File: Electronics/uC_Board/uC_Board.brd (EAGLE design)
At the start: 30.8 x 54.6 mm, 11 parts, among them IC1 74LS241N, J1 1, J2 SCREW-TERMINAL-2P-3470070P1, J3 2, J4 3

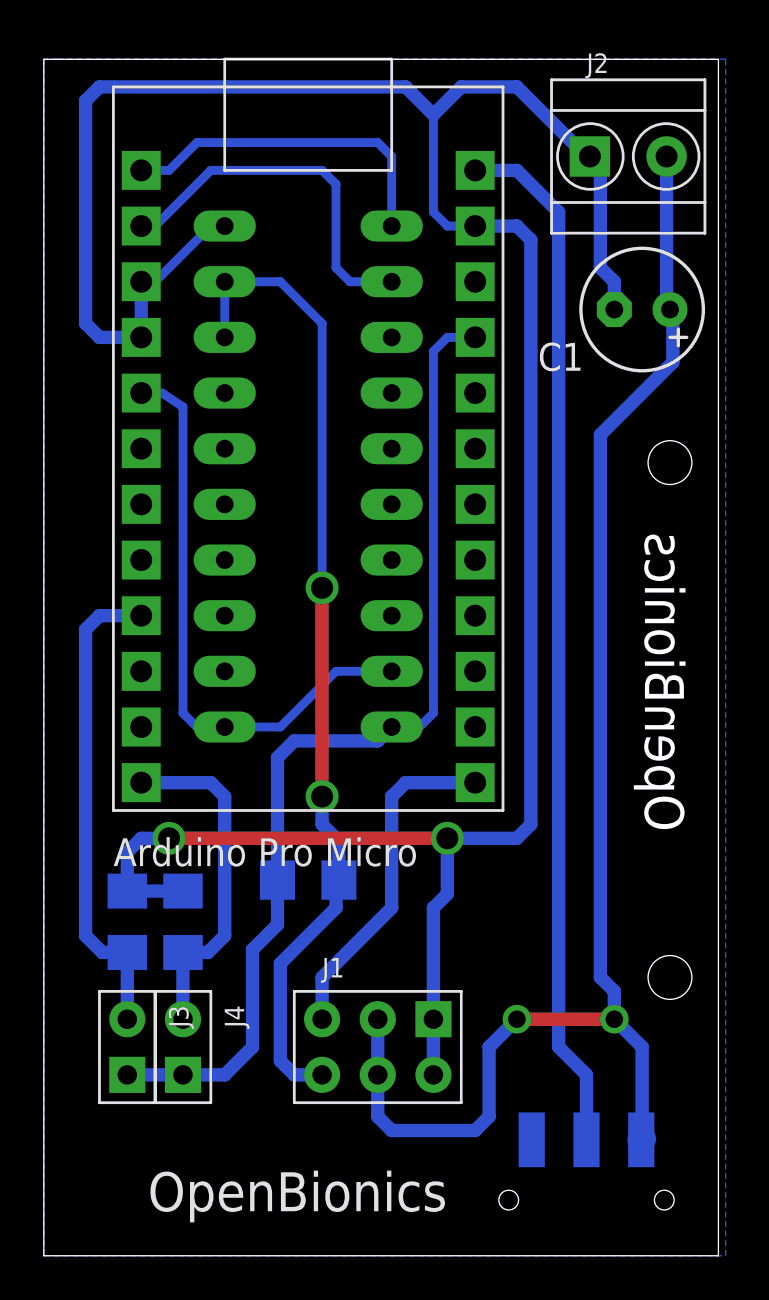
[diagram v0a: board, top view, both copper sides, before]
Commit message: Repair the Bottom Silkscreen of uC_Board PCB.
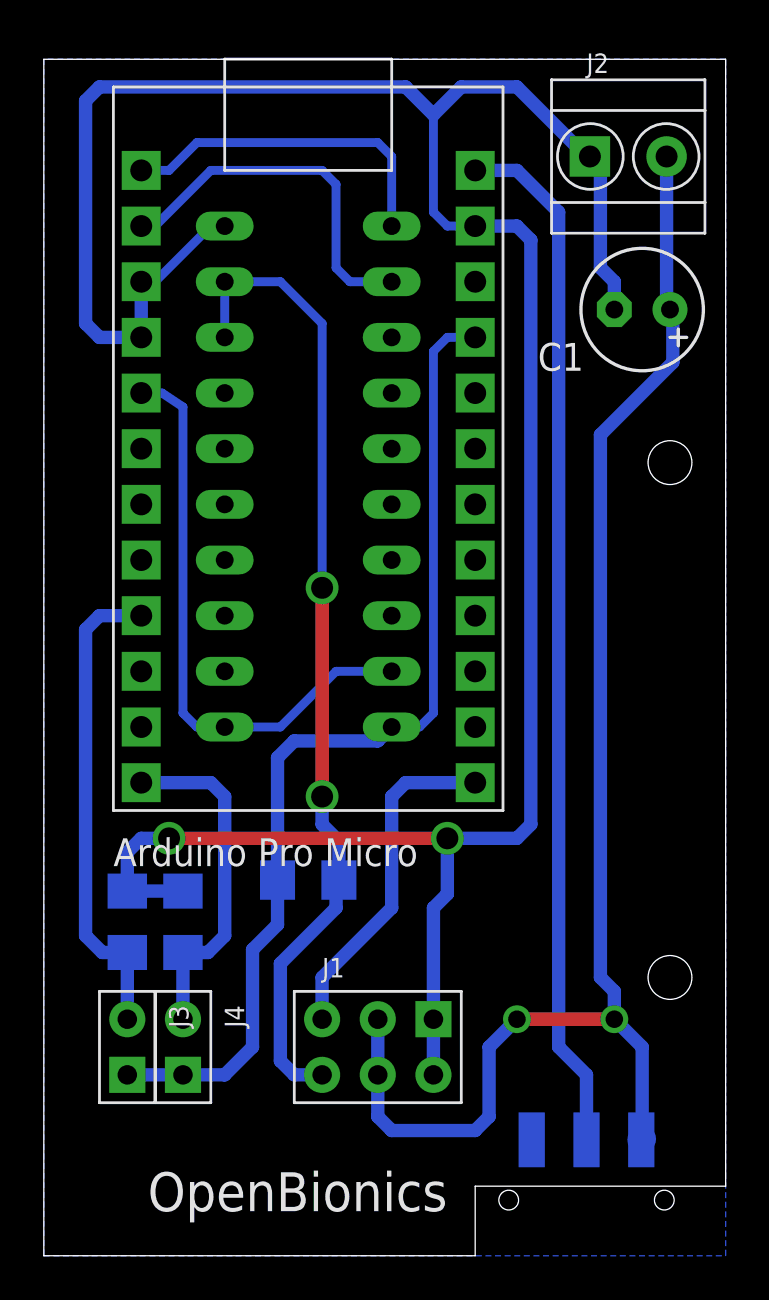
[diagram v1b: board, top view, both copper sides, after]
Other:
- board size 30.8 x 54.6 mm -> 31.1 x 54.6 mm
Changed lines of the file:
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@@
 <?xml version="1.0" encoding="utf-8"?>
 <!DOCTYPE eagle SYSTEM "eagle.dtd">
-<eagle version="7.1.0">
+<eagle version="7.2.0">
 <drawing>
 <settings>
@@
 <board>
 <plain>
-<wire x1="35.56" y1="15.24" x2="66.345" y2="15.24" width="0" layer="20"/>
-<wire x1="66.345" y1="15.24" x2="66.345" y2="69.84" width="0" layer="20"/>
-<wire x1="66.345" y1="69.84" x2="35.56" y2="69.84" width="0" layer="20"/>
+<wire x1="66.6625" y1="69.84" x2="35.56" y2="69.84" width="0" layer="20"/>
 <wire x1="35.56" y1="69.84" x2="35.56" y2="15.24" width="0" layer="20"/>
 <hole x="64.135" y="51.435" drill="2"/>
 <hole x="64.135" y="27.94" drill="2"/>
-<text x="64.77" y="48.26" size="1.778" layer="20" font="vector" ratio="18" rot="MR270">OpenBionics</text>
+<text x="64.77" y="48.26" size="1.778" layer="22" font="vector" ratio="18" rot="MR270">OpenBionics</text>
 <text x="53.975" y="19.05" size="1.778" layer="21" font="vector" ratio="18" rot="R180">OpenBionics</text>
+<wire x1="35.56" y1="15.24" x2="55.245" y2="15.24" width="0" layer="20"/>
+<wire x1="55.245" y1="15.24" x2="55.245" y2="18.415" width="0" layer="20"/>
+<wire x1="55.245" y1="18.415" x2="66.675" y2="18.415" width="0" layer="20"/>
+<wire x1="66.675" y1="18.415" x2="66.675" y2="69.85" width="0" layer="20"/>
 </plain>
 <attributes>
@@
 </class>
 </classes>
-<designrules name="SparkFun">
+<designrules name="SeeedStudio_2layer_DRU_no_angle_20140221">
+<description language="de">&lt;b&gt;EAGLE Design Rules&lt;/b&gt;
+&lt;p&gt;
+Die Standard-Design-Rules sind so gewählt, dass sie für
+die meisten Anwendungen passen. Sollte ihre Platine
+besondere Anforderungen haben, treffen Sie die erforderlichen
+Einstellungen hier und speichern die Design Rules unter
+einem neuen Namen ab.</description>
 <description language="en">&lt;b&gt;EAGLE Design Rules&lt;/b&gt;
 &lt;p&gt;
@@
 necessary adjustments and save your customized
 design rules under a new name.</description>
+<description language="zh">&lt;b&gt;Seeed Studio EAGLE Design Rules&lt;/b&gt;
+</description>
 <param name="layerSetup" value="(1*16)"/>
-<param name="mtCopper" value="0.035mm 0.035mm 0.035mm 0.035mm 0.035mm 0.035mm 0.035mm 0.035mm 0.035mm 0.035mm 0.035mm 0.035mm 0.035mm 0.035mm 0.035mm 0.035mm"/>
-<param name="mtIsolate" value="1.5mm 0.15mm 0.2mm 0.15mm 0.2mm 0.15mm 0.2mm 0.15mm 0.2mm 0.15mm 0.2mm 0.15mm 0.2mm 0.15mm 0.2mm"/>
-<param name="mdWireWire" value="8mil"/>
-<param name="mdWirePad" value="8mil"/>
-<param name="mdWireVia" value="8mil"/>
-<param name="mdPadPad" value="8mil"/>
-<param name="mdPadVia" value="8mil"/>
-<param name="mdViaVia" value="8mil"/>
-<param name="mdSmdPad" value="8mil"/>
-<param name="mdSmdVia" value="8mil"/>
-<param name="mdSmdSmd" value="8mil"/>
+<param name="mtCopper" value="0.035mm 0.0175mm 0.035mm 0.035mm 0.035mm 0.035mm 0.035mm 0.035mm 0.035mm 0.035mm 0.035mm 0.035mm 0.035mm 0.035mm 0.0175mm 0.035mm"/>
+<param name="mtIsolate" value="1.5mm 1.1mm 0.2mm 0.15mm 0.2mm 0.15mm 0.2mm 0.15mm 0.2mm 0.15mm 0.2mm 0.15mm 0.2mm 0.15mm 0.2mm"/>
+<param name="mdWireWire" value="6mil"/>
+<param name="mdWirePad" value="6mil"/>
+<param name="mdWireVia" value="6mil"/>
+<param name="mdPadPad" value="6mil"/>
+<param name="mdPadVia" value="6mil"/>
+<param name="mdViaVia" value="6mil"/>
+<param name="mdSmdPad" value="0mil"/>
+<param name="mdSmdVia" value="0mil"/>
+<param name="mdSmdSmd" value="0mil"/>
 <param name="mdViaViaSameLayer" value="8mil"/>
 <param name="mnLayersViaInSmd" value="2"/>
-<param name="mdCopperDimension" value="8mil"/>
-<param name="mdDrill" value="8mil"/>
+<param name="mdCopperDimension" value="10mil"/>
+<param name="mdDrill" value="10mil"/>
 <param name="mdSmdStop" value="0mil"/>
-<param name="msWidth" value="8mil"/>
-<param name="msDrill" value="20mil"/>
-<param name="msMicroVia" value="9.99mm"/>
+<param name="msWidth" value="6mil"/>
+<param name="msDrill" value="12mil"/>
+<param name="msMicroVia" value="12mil"/>
 <param name="msBlindViaRatio" value="0.5"/>
 <param name="rvPadTop" value="0.25"/>
@@
 <param name="rvMicroViaOuter" value="0.25"/>
 <param name="rvMicroViaInner" value="0.25"/>
-<param name="rlMinPadTop" value="12mil"/>
+<param name="rlMinPadTop" value="10mil"/>
 <param name="rlMaxPadTop" value="20mil"/>
 <param name="rlMinPadInner" value="10mil"/>
 <param name="rlMaxPadInner" value="20mil"/>
-<param name="rlMinPadBottom" value="12mil"/>
+<param name="rlMinPadBottom" value="10mil"/>
 <param name="rlMaxPadBottom" value="20mil"/>
-<param name="rlMinViaOuter" value="10mil"/>
+<param name="rlMinViaOuter" value="6mil"/>
 <param name="rlMaxViaOuter" value="20mil"/>
-<param name="rlMinViaInner" value="10mil"/>
+<param name="rlMinViaInner" value="6mil"/>
 <param name="rlMaxViaInner" value="20mil"/>
 <param name="rlMinMicroViaOuter" value="4mil"/>
@@
 <param name="psTop" value="-1"/>
 <param name="psBottom" value="-1"/>
-<param name="psFirst" value="-1"/>
+<param name="psFirst" value="0"/>
 <param name="psElongationLong" value="100"/>
 <param name="psElongationOffset" value="100"/>
 <param name="mvStopFrame" value="1"/>
 <param name="mvCreamFrame" value="0"/>
-<param name="mlMinStopFrame" value="4mil"/>
-<param name="mlMaxStopFrame" value="4mil"/>
+<param name="mlMinStopFrame" value="2mil"/>
+<param name="mlMaxStopFrame" value="2mil"/>
 <param name="mlMinCreamFrame" value="0mil"/>
 <param name="mlMaxCreamFrame" value="0mil"/>
-<param name="mlViaStopLimit" value="20mil"/>
+<param name="mlViaStopLimit" value="100mil"/>
 <param name="srRoundness" value="0"/>
 <param name="srMinRoundness" value="0mil"/>
@@
 <param name="checkAngle" value="0"/>
 <param name="checkFont" value="1"/>
-<param name="checkRestrict" value="1"/>
+<param name="checkRestrict" value="0"/>
 <param name="useDiameter" value="13"/>
 <param name="maxErrors" value="50"/>
@@
 <wire x1="43.18" y1="62.23" x2="43.815" y2="62.23" width="0.4064" layer="16"/>
 <polygon width="0.6096" layer="16" isolate="1.27">
-<vertex x="36.195" y="69.85"/>
+<vertex x="66.675" y="69.85"/>
 <vertex x="35.56" y="69.85"/>
 <vertex x="35.56" y="15.24"/>
 <vertex x="66.675" y="15.24"/>
-<vertex x="66.675" y="69.85"/>
 </polygon>
 <contactref element="J2" pad="1"/>
